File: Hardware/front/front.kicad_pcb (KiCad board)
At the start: 4 copper layers, 177 x 61 mm, 71 parts, among them J102 Conn_02x25_Counter_Clockwise, J301 Conn_02x25_Counter_Clockwise, Q301 2N7002E, Q302 2N7002E, SW201 B3W-9002-Y1C, SW202 B3W-9002-Y1C, SW203 B3W-9002-Y1C, SW204 B3W-9002-Y1C, SW205 B3W-9000-RHG2C, SW206 B3W-9002-G1G, SW207 TT EN11, U101 PCA9535PW, U102 AT24CS32-XHM, U103 PCA9955B, U201 74LV14, U202 74LVC1G14GV

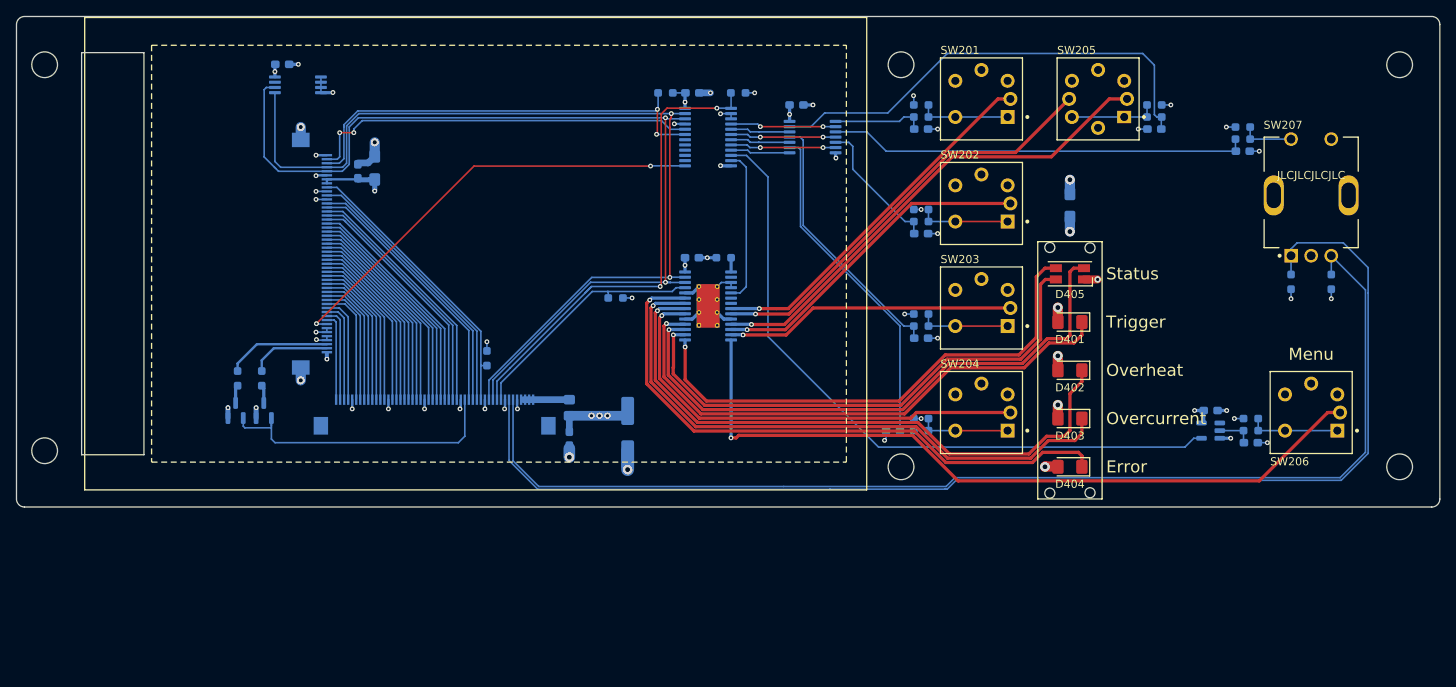
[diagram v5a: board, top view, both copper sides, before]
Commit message: Minor tweaks to front panel & controller for manufacture
- Create footprint for JLCPCB assembly tooling holes

- Added tooling holes to front panel board and fixed ERC errors

- Added tooling holes to controller

- Moved a few traces on controller board and fixed a few broken package
  associations

- Add pull-up on Ethernet PHY's reset line (so when the SoM boots, we're
  not making it angerey)

- Fixed order of BOOTx pins to DIP switch

- Fixed swapped USB host/device pins

- Fixed swapped ETH_TXP/ETH_TXN pair on when exiting the CPU sheet and
  connecting to the rear IO sheet (in the main sheet of the schematic)
  and the associated incorrect resistors/caps
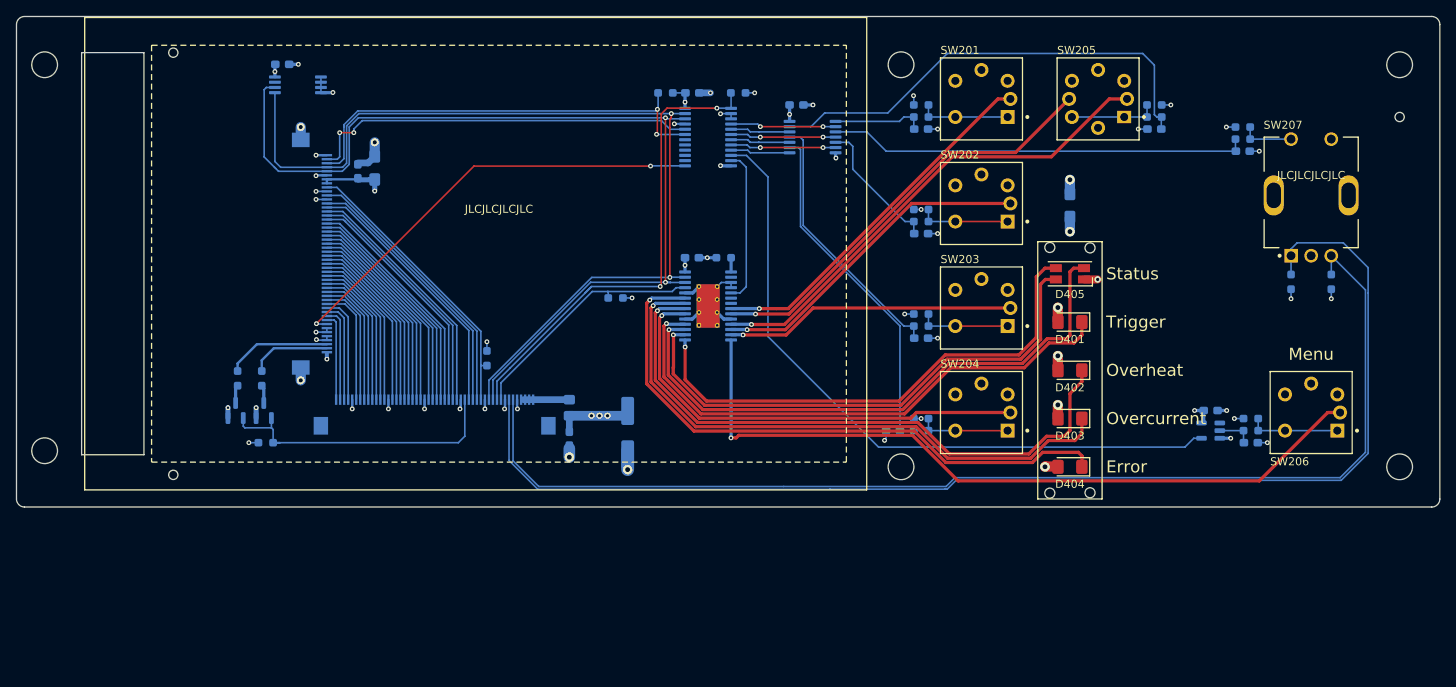
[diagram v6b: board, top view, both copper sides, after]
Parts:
- added H107: MountingHole, programmable-load:JLCPCB-SmdAssembly-ToolingHole, F.Cu at (57.5, 23.5)
- added H108: MountingHole, programmable-load:JLCPCB-SmdAssembly-ToolingHole, F.Cu at (57.5, 76.0)
- added H109: MountingHole, programmable-load:JLCPCB-SmdAssembly-ToolingHole, F.Cu at (210.0, 31.5)
- added R304: 10k, Resistor_SMD:R_0603_1608Metric_Pad0.98x0.95mm_HandSolder, B.Cu at (69.0, 72.0)
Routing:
- net +3V3: track 57.8 -> 59.0 mm, vias 31 -> 32

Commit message: Rev4 front panel (#3)
* hw: start work on new front panel board

- This replaces all the various I2C chips with a single RP2040 (with
  some boot flash) to handle scanning the keyboard, driving PWM LEDs
  (including the display backlight) and actually handling the display
  controller initialization.

- Flipped the pinout of the connector to the main controller board

* hw: more front panel stuff

- fixed the mirrored pinout for the connector to the controller board

- Replaced a few capacitors to reduce BOM count

- Start connecting signals to RP2040, including the flash connection
  (dedicated to it)

* hw: First pass at new front panel

- Finished routing all signals on the front panel

- Put back the LED controller (PCA9955B) since that's a very nice and
  convenient way to drive the LEDs; it's driven via a "private" I2C bus
  from the RP2040 instead of the host controlling it.

  The touch panel controller is also hanging off this private bus so we
  can deal with it.

- Made trigger LED bicolor (green/orange)

* hw: minor front panel tweaks

* updated front panel pinout

- added system reset, direct load on/off switch output lines

- added separate touch screen reset/interrupt lines (the touch
  controller gets to be driven by linux side)

- update footprint for ER-TFT040-1 display

  this tweaks the sizes of the openings and the text labels a bit to be
  prettier

* swap touch irq/reset lines to match controller
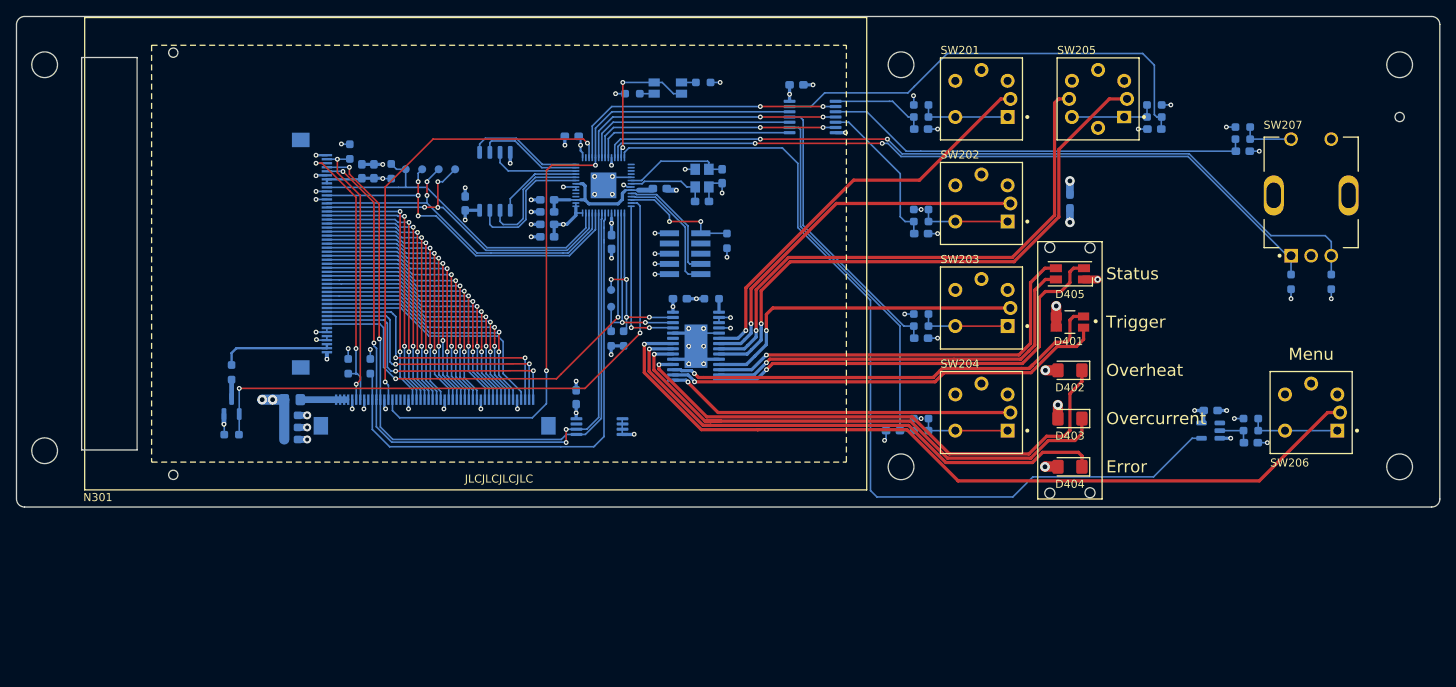
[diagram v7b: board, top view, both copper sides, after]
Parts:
- removed C106: 100nF, Capacitor_SMD:C_0603_1608Metric_Pad1.08x0.95mm_HandSolder
- removed C303: 10µF, Capacitor_Tantalum_SMD:CP_EIA-3216-18_Kemet-A_Pad1.58x1.35mm_HandSolder
- removed Q302: 2N7002E, Package_TO_SOT_SMD:SOT-23
- removed R104, R303: 10k, Resistor_SMD:R_0603_1608Metric_Pad0.98x0.95mm_HandSolder
- removed the REF** at (98.0, 48.5)
- removed U103: PCA9955B, Package_SO:HTSSOP-28-1EP_4.4x9.7mm_P0.65mm_EP2.85x5.4mm_ThermalVias
- added C103: 22µF, Capacitor_SMD:C_0603_1608Metric_Pad1.08x0.95mm_HandSolder, B.Cu at (72.2, 71.6)
- added C301: 4.7µF, Capacitor_SMD:C_0603_1608Metric_Pad1.08x0.95mm_HandSolder, B.Cu at (82.5, 38.2)
- added C501: 100nF, Capacitor_SMD:C_0603_1608Metric_Pad1.08x0.95mm_HandSolder, B.Cu at (104.0, 44.9)
- added C502: 4.7µF, Capacitor_SMD:C_0603_1608Metric_Pad1.08x0.95mm_HandSolder, B.Cu at (104.0, 46.4)
- added C503: 100nF, Capacitor_SMD:C_0603_1608Metric_Pad1.08x0.95mm_HandSolder, B.Cu at (112.0, 47.0)
- added C504: 100nF, Capacitor_SMD:C_0603_1608Metric_Pad1.08x0.95mm_HandSolder, B.Cu at (104.0, 41.8)
- added C505: 100nF, Capacitor_SMD:C_0603_1608Metric_Pad1.08x0.95mm_HandSolder, B.Cu at (118.0, 40.4)
- added C506: 4.7µF, Capacitor_SMD:C_0603_1608Metric_Pad1.08x0.95mm_HandSolder, B.Cu at (104.0, 43.3)
- added C507: 100nF, Capacitor_SMD:C_0603_1608Metric_Pad1.08x0.95mm_HandSolder, B.Cu at (107.0, 33.9)
- added C508: 100nF, Capacitor_SMD:C_0603_1608Metric_Pad1.08x0.95mm_HandSolder, B.Cu at (93.8, 42.2)
- added C509: 18pF, Capacitor_SMD:C_0603_1608Metric_Pad1.08x0.95mm_HandSolder, B.Cu at (123.2, 42.0)
- added C510: 18pF, Capacitor_SMD:C_0603_1608Metric_Pad1.08x0.95mm_HandSolder, B.Cu at (125.8, 38.9)
- added D501: LED_Dual_AAKK, programmable-load:LED-3227, B.Cu at (119.0, 27.9)
- added J501: Conn_ARM_JTAG_SWD_10, Connector_PinHeader_1.27mm:PinHeader_2x05_P1.27mm_Vertical_SMD, B.Cu at (121.2, 48.5)
- added N301: ER-TFT040-1, programmable-load:ER-TFT040-1, F.Cu at (98.0, 48.5)
- added R305: 10k, Resistor_SMD:R_0603_1608Metric_Pad0.98x0.95mm_HandSolder, B.Cu at (84.6, 38.2)
- added R501: 10k, Resistor_SMD:R_0603_1608Metric_Pad0.98x0.95mm_HandSolder, B.Cu at (126.3, 46.9)
- added R502: 1k, Resistor_SMD:R_0603_1608Metric_Pad0.98x0.95mm_HandSolder, B.Cu at (114.6, 28.6)
- added R503: 1k, Resistor_SMD:R_0603_1608Metric_Pad0.98x0.95mm_HandSolder, B.Cu at (123.4, 27.2)
- added R504: 2k2, Resistor_SMD:R_0603_1608Metric_Pad0.98x0.95mm_HandSolder, B.Cu at (112.0, 59.0)
- added R505: 2k2, Resistor_SMD:R_0603_1608Metric_Pad0.98x0.95mm_HandSolder, B.Cu at (113.5, 59.0)
- added TP301: /SPI_CS, TestPoint:TestPoint_Pad_D1.0mm, B.Cu at (86.4, 38.0)
- added TP302: SPI_SCK, TestPoint:TestPoint_Pad_D1.0mm, B.Cu at (88.5, 38.0)
- added TP303: SPI_MOSI, TestPoint:TestPoint_Pad_D1.0mm, B.Cu at (90.5, 38.0)
- added TP304: SPI_MISO, TestPoint:TestPoint_Pad_D1.0mm, B.Cu at (92.5, 38.0)
- added TP501: I²C_SCL, TestPoint:TestPoint_Pad_D1.0mm, B.Cu at (112.0, 55.1)
- added TP502: I²C_SDA, TestPoint:TestPoint_Pad_D1.0mm, B.Cu at (112.0, 53.0)
- added U501: RP2040, Package_DFN_QFN:QFN-56-1EP_7x7mm_P0.4mm_EP3.2x3.2mm, B.Cu at (111.0, 40.0)
- added U502: W25Q128JVS, Package_SO:SOIC-8_5.23x5.23mm_P1.27mm, B.Cu at (97.5, 39.5)
- added Y501: 12MHz, Crystal:Crystal_SMD_3225-4Pin_3.2x2.5mm, B.Cu at (123.2, 39.1)
- C102: value 33µF -> 22µF; footprint Capacitor_SMD:CP_Elec_6.3x5.7 -> Capacitor_SMD:C_0603_1608Metric_Pad1.08x0.95mm_HandSolder
- C401: value 10µF -> 4.7µF; footprint Capacitor_Tantalum_SMD:CP_EIA-3216-18_Kemet-A_Pad1.58x1.35mm_HandSolder -> Capacitor_SMD:C_0603_1608Metric_Pad1.08x0.95mm_HandSolder
- D401: value Green -> LED_Dual_AAKK; footprint LED_SMD:LED_1206_3216Metric_Pad1.42x1.75mm_HandSolder -> programmable-load:LED-3227
- Q301: value 2N7002E -> AO3400A
- R301: value 3R6 -> 2R2
- R302: value 3R6 -> 10k
- U101: value PCA9535PW -> PCA9955B; footprint Package_SO:TSSOP-24_4.4x7.8mm_P0.65mm -> Package_SO:HTSSOP-28-1EP_4.4x9.7mm_P0.65mm_EP2.85x5.4mm
- moved R102 57.0 mm to (82.0, 62.5), turned to 90 degrees
- moved U102 56.7 mm to (110.5, 70.0)
- moved C105 55.2 mm to (107.6, 66.3), turned to 90 degrees
- moved C102 41.9 mm to (72.2, 70.1), turned to 0 degrees
- moved C101 34.7 mm to (72.2, 68.6), turned to 0 degrees
- moved FB101 34.5 mm to (72.3, 66.7), turned to 180 degrees
- moved R103 34.3 mm to (79.2, 62.5), turned to 90 degrees
- moved R302 30.3 mm to (79.5, 35.8), turned to 90 degrees
- moved U101 26.0 mm to (122.5, 60.0)
- moved C104 25.6 mm to (120.5, 54.1), turned to 0 degrees
- moved R101 5.32 mm to (124.5, 54.1)
- moved R304 4.37 mm to (64.8, 71.0)
- moved C206 2.50 mm to (135.0, 27.5)
- moved U201 2.50 mm to (137.0, 31.5)
- moved R301 1.06 mm to (64.8, 63.2)
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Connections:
- C104 pad 1: GND -> +3V3
- C104 pad 2: +3V3 -> GND
- D401 pad 1: /LED_TRIGGER -> +3V3
- FB101 pad 1: Net-(J102-Pin_1) -> Net-(J102-Pin_47)
- J102 pad 1: Net-(J102-Pin_1) -> /DISP_VSYNC
- J102 pad 10: /~{IRQ} -> /R3
- J102 pad 11: /SCL -> /R2
- J102 pad 12: /SDA -> /R1
- J102 pad 13: GND -> /R0
- J102 pad 14: /~{SPI_CS} -> GND
- J102 pad 15: /SPI_SCK -> /G7
- J102 pad 16: /SPI_MOSI -> /G6
- J102 pad 17: /SPI_MISO -> /G5
- J102 pad 18: /DISP_PWM -> /G4
- J102 pad 19: GND -> /G3
- J102 pad 2: Net-(J102-Pin_1) -> /DISP_HSYNC
- J102 pad 20: /B0 -> /G2
- J102 pad 21: /B1 -> /G1
- J102 pad 22: /B2 -> /G0
- J102 pad 23: /B3 -> GND
- J102 pad 24: /B4 -> /B7
- J102 pad 25: /B5 -> /B6
- J102 pad 26: /B6 -> /B5
- J102 pad 27: /B7 -> /B4
- J102 pad 28: GND -> /B3
- J102 pad 29: /G0 -> /B2
- J102 pad 3: Net-(J102-Pin_1) -> /DISP_PCLK
- J102 pad 30: /G1 -> /B1
- J102 pad 31: /G2 -> /B0
- J102 pad 32: /G3 -> GND
- J102 pad 33: /G4 -> unconnected-(J102-Pin_33)
- J102 pad 34: /G5 -> unconnected-(J102-Pin_34)
- J102 pad 35: /G6 -> unconnected-(J102-Pin_35)
- J102 pad 36: /G7 -> /SW_ENABLE
- J102 pad 37: GND -> /~{SYS_RESET}
- J102 pad 38: /R0 -> GND
- J102 pad 39: /R1 -> /SDA
- J102 pad 4: Net-(J102-Pin_1) -> /DISP_DE
- J102 pad 40: /R2 -> /SCL
- J102 pad 41: /R3 -> /~{HOST_IRQ}
- J102 pad 42: /R4 -> unconnected-(J102-Pin_42)
- J102 pad 43: /R5 -> GND
- J102 pad 44: /R6 -> /~{TOUCH_IRQ}
- J102 pad 45: /R7 -> /~{TOUCH_RESET}
- J102 pad 47: /DISP_DE -> Net-(J102-Pin_47)
- J102 pad 48: /DISP_PCLK -> Net-(J102-Pin_47)
- J102 pad 49: /DISP_HSYNC -> Net-(J102-Pin_47)
- J102 pad 50: /DISP_VSYNC -> Net-(J102-Pin_47)
- J102 pad 6: /ENCODER_B -> /R7
- J102 pad 7: /ENCODER_A -> /R6
- J102 pad 8: GND -> /R5
- J102 pad 9: /~{RESET} -> /R4
- J301 pad 2: /LCD, Backlight driver/LEDK1 -> /LCD, Backlight driver/LEDK
- J301 pad 3: /LCD, Backlight driver/LEDK2 -> /LCD, Backlight driver/LEDK
- J301 pad MP: GND -> (no net)
- R101 pad 2: Net-(U103-REXT) -> Net-(U101-REXT)
- R102 pad 1: /~{IRQ} -> /~{HOST_IRQ}
- R103 pad 1: /~{RESET} -> /~{TOUCH_IRQ}
- R301 pad 1: /LCD, Backlight driver/LEDK2 -> /LCD, Backlight driver/LEDK
- R302 pad 1: /LCD, Backlight driver/LEDK1 -> /~{TOUCH_RESET}
- R302 pad 2: Net-(Q302-D) -> +3V3
- R304 pad 2: +3V3 -> GND
- U101 pad 1: /~{IRQ} -> Net-(U101-REXT)
- U101 pad 10: /SW_MENU -> GND
- U101 pad 11: /~{LED_OE} -> /LED_MODE_CW
- U101 pad 12: GND -> /LED_STATUS_G
- U101 pad 13: /~{DISP_RESET} -> /LED_STATUS_B
- U101 pad 14: unconnected-(U101-IO1_1) -> /LED_STATUS_R
- U101 pad 15: unconnected-(U101-IO1_2) -> /LED_MODE_EXT
- U101 pad 16: unconnected-(U101-IO1_3) -> /LED_TRIGGER2
- U101 pad 17: unconnected-(U101-IO1_4) -> /LED_TRIGGER1
- U101 pad 18: unconnected-(U101-IO1_5) -> /LED_OVRHEAT
- U101 pad 19: /~{TOUCH_IRQ} -> GND
- U101 pad 20: /~{TOUCH_RESET} -> /LED_OVRCURR
- U101 pad 21: GND -> /LED_ERROR
- U101 pad 22: /SCL -> /LED_MENU
- U101 pad 23: /SDA -> unconnected-(U101-LED15)
- U101 pad 24: +3V3 -> GND
- U101 pad 4: /SW_MODE_CC -> +3V3
- U101 pad 5: /SW_ENABLE -> GND
- U101 pad 6: /SW_ENCODER -> /LED_MODE_CC
- U101 pad 7: /SW_MODE_CW -> /LED_MODE_CV
- U101 pad 8: /SW_MODE_CV -> /LED_EN_G
- U101 pad 9: /SW_MODE_EXT -> /LED_EN_R
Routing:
- net /SW_ENABLE: track 7.41 -> 86.6 mm, vias 0 -> 2
- net /LED_TRIGGER: track 68.7 -> 0.00 mm, vias 1 -> 0
- net /~{HOST_IRQ}: track 0.00 -> 65.0 mm
- net /ENCODER_A: track 155.2 -> 93.4 mm, vias 0 -> 2
- net /~{IRQ}: track 61.0 -> 0.00 mm, vias 2 -> 0
- net /LED_TRIGGER1: track 0.00 -> 56.4 mm, vias 0 -> 1
- net /~{SYS_RESET}: track 0.00 -> 56.3 mm, vias 0 -> 2
- net /LED_TRIGGER2: track 0.00 -> 55.1 mm, vias 0 -> 1
- net /ENCODER_B: track 145.2 -> 100.4 mm, vias 0 -> 2
- net /DISP_PWM: track 37.1 -> 75.6 mm, vias 0 -> 2
- net /~{RESET}: track 30.7 -> 0.00 mm
- net /SCL: track 120.7 -> 91.7 mm, vias 2 -> 4
- net /SW_MENU: track 85.6 -> 112.2 mm
- net /SDA: track 117.9 -> 91.5 mm
- net /DISP_SCL: track 0.00 -> 24.4 mm, vias 0 -> 2
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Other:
- board text added: "Rev 4"
- board text removed: "Rev 3"

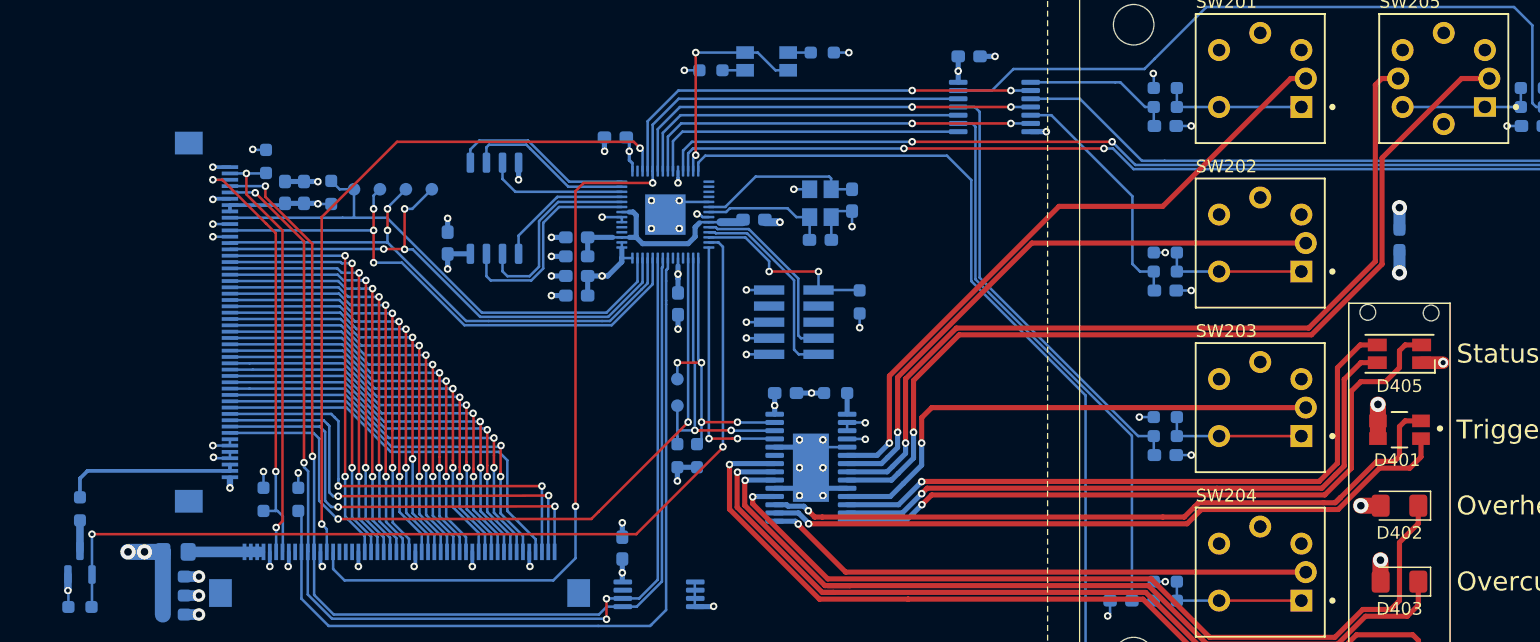
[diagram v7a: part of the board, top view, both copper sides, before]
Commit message: front: minor tweaks
- added some more pull-ups on IO lines

- doubled decoupling capacitance for LEDs
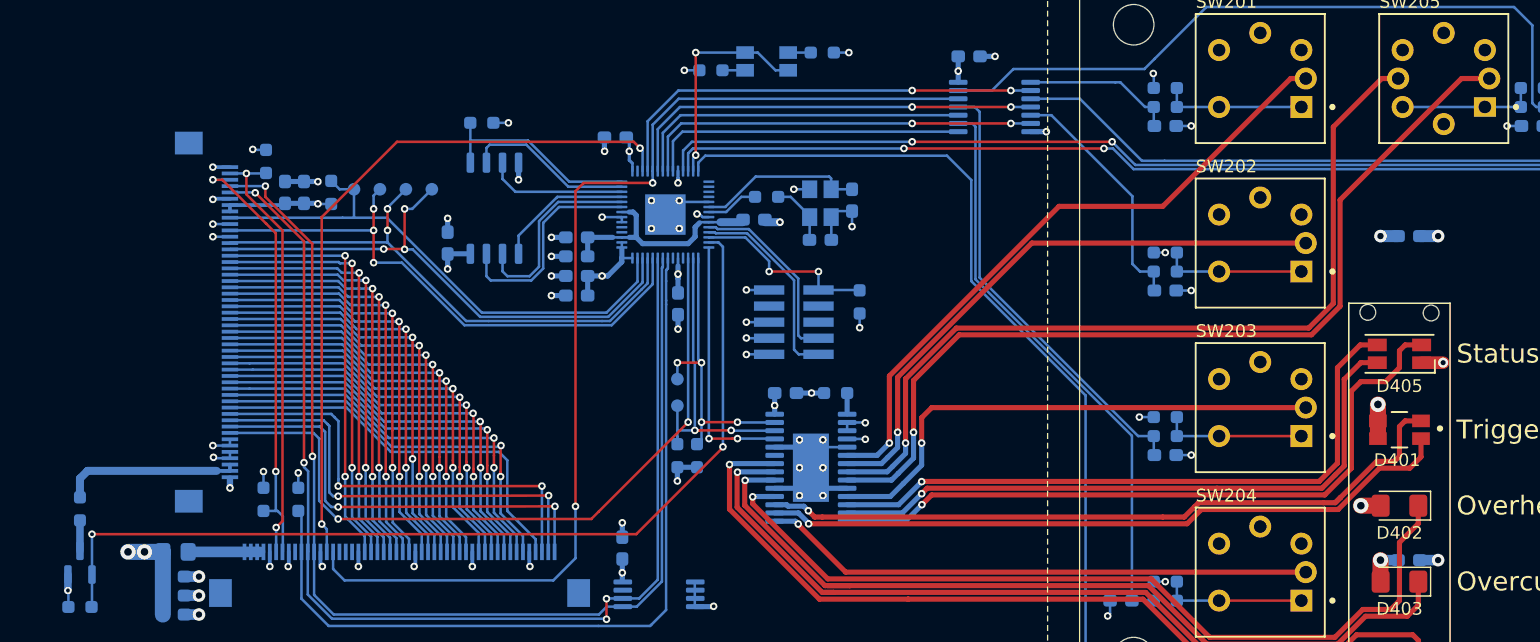
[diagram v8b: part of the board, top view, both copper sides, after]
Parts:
- added C402: 4.7µF, Capacitor_SMD:C_0603_1608Metric_Pad1.08x0.95mm_HandSolder, B.Cu at (169.8, 67.3)
- added R506: 1k, Resistor_SMD:R_0603_1608Metric_Pad0.98x0.95mm_HandSolder, B.Cu at (119.0, 38.6)
- added R507: 10k, Resistor_SMD:R_0603_1608Metric_Pad0.98x0.95mm_HandSolder, B.Cu at (96.5, 32.8)
- C509, C510: value 18pF -> 22pF
- moved C401 0.81 mm to (169.8, 41.7), turned to 0 degrees
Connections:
- C509 pad 1: /Embedded Controller/XOUT -> Net-(C509-Pad1)
- Y501 pad 3: /Embedded Controller/XOUT -> Net-(C509-Pad1)
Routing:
- net /Embedded Controller/XOUT: track 10.2 -> 4.15 mm
- net Net-(C509-Pad1): track 0.00 -> 5.01 mm
- net +3V3: track 81.4 -> 83.6 mm, vias 41 -> 42
- net /Embedded Controller/~{FLASH_CS}: track 14.7 -> 16.6 mm
- net GND: track 78.6 -> 79.7 mm, vias 56 -> 57
